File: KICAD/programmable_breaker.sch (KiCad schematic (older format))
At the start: 44 parts

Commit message: merge nicolas & stef
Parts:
- removed Q? (x2): BC847, Package_TO_SOT_SMD:SOT-23, symbol Transistor_BJT:BC847
- removed R? (x2): 10k, symbol Device:R
- removed U? (x3): LM7332, symbol Amplifier_Operational:LM7332
- added U? (x3): LM2903, Package_SO:SOIC-8-1EP_3.9x4.9mm_P1.27mm_EP2.29x3mm, symbol Comparator:LM2903
- 3214W: renamed from RV?; value R_POT -> 10K; footprint (none) -> Potentiometer_SMD:Potentiometer_Bourns_3214W_Vertical
- C? (x2): footprint (none) -> Capacitor_SMD:C_0805_2012Metric_Pad1.15x1.40mm_HandSolder
- C? (x2): value C -> 10n; footprint (none) -> Capacitor_SMD:C_0805_2012Metric_Pad1.15x1.40mm_HandSolder
- C? (x2): value 100n -> 470n; footprint (none) -> Capacitor_SMD:C_0805_2012Metric_Pad1.15x1.40mm_HandSolder
- R? (x16): footprint (none) -> Resistor_SMD:R_0805_2012Metric_Pad1.20x1.40mm_HandSolder
- R? (x2): value R -> 100k; footprint (none) -> Resistor_SMD:R_0805_2012Metric_Pad1.20x1.40mm_HandSolder
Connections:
- wire segments 89 -> 81
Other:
- note added: "comparateur courant\n(Sur-courant)"
- note removed: "Col. ouvert ?"
- note removed: "Softstart > 10ms a 100ms (le plus lent)"
- note removed: "Tres petit (Pics intempestifs) env 1ms"

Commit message: revex with jmt
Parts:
- removed SLD1, SLD2: SESAME_SHIELD, symbol Sesame:SESAME_SHIELD
- R?: value R -> 9.1k
- R?: value R -> 1k
- R? (x2): value R -> 4.7k
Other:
- note removed: "————————————————————————————————————————————————\nENTREE(S):\nTrigger quand la meusure selectionné depasse le seuil maximal\nVoltage_Sens_R | Entree Analogique | Tension mesurée du coté Droit (Provenant du block Voltage Current Sens Right)\nCurrent_Sens_R | Entree Analogique | Courant mesuré du coté Droit (Provenant du block Voltage Current Sens Right)\nVoltage_Sens_L | Entree Analogique | Tensio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"
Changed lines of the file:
@@
 $Descr A4 11693 8268
 encoding utf-8
-Sheet 5 16
+Sheet 4 16
 Title "SESAME"
 Date ""
@@
 Comment4 ""
 $EndDescr
-Text Notes 450  -300 0    50   ~ 0
-————————————————————————————————————————————————\nENTREE(S):\nTrigger quand la meusure selectionné depasse le seuil maximal\nVoltage_Sens_R | Entree Analogique | Tension mesurée du coté Droit (Provenant du block Voltage Current Sens Right)\nCurrent_Sens_R | Entree Analogique | Courant mesuré du coté Droit (Provenant du block Voltage Current Sens Right)\nVoltage_Sens_L | Entree Analogique | Tension mesurée du coté Gauche (Provenant du block Voltage Current Sens Left)\nCurrent_Sens_L | Entree Analogique | Courant mesuré du coté Gauche (Provenant du block Voltage Current Sens Left)\nDir | Entrée Numérique | Sens du courant et par extension choix de la meusure Droite / Gauche\nCurrent_Thres | Entrée ext. Analogique | Seuil externe qui definir le courant maximal\nVoltage_Thres | Entrée ext. Analogique | Seuil externe qui definir la tension maximale\nRearm | Entrée ext. Numerique | Rearmer le disjoncteur\nTrigger_Breaker | Entrée ext. Numerique | Singnal externe de declenchement du disjoncteur\n————————————————————————————————————————————————\nSORTIE(S):\nShutdown | Sortie Numerique | Signal de coupure des MOS\n
-$Comp
-L Sesame:SESAME_SHIELD SLD1
-U 2 1 618C4894
-P 5800 -1400
-F 0 "SLD1" H 5450 -1150 50  0000 L CNN
-F 1 "SESAME_SHIELD" H 5300 -1250 50  0000 L CNN
-F 2 "" H 5950 -2650 50  0001 C CNN
-F 3 "" H 5950 -2650 50  0001 C CNN
-	2    5800 -1400
-	1    0    0    -1
-$EndComp
-$Comp
-L Sesame:SESAME_SHIELD SLD2
-U 1 1 618C53DC
-P 6250 -1400
-F 0 "SLD2" H 7308 -1135 50  0000 C CNN
-F 1 "SESAME_SHIELD" H 7308 -1226 50  0000 C CNN
-F 2 "" H 6400 -2650 50  0001 C CNN
-F 3 "" H 6400 -2650 50  0001 C CNN
-	1    6250 -1400
-	1    0    0    -1
-$EndComp
-Text HLabel 5800 3200 0    50   Input ~ 0
-Rearm
 Text HLabel 2100 2400 0    50   Input ~ 0
 Voltage_Sens
@@
 Wire Wire Line
 	3000 7200 3200 7200
-Wire Wire Line
-	5800 3200 6600 3200
-Wire Wire Line
-	6600 2550 6600 3200
 Text Notes 4900 3000 2    49   ~ 0
 comparateur tension\n(Sur-tension)
@@
 Wire Wire Line
 	7400 2200 7300 2200
-Connection ~ 6600 2550
 Wire Wire Line
 	6600 2550 6850 2550
@@
 Wire Wire Line
 	7300 2550 7550 2550
-Connection ~ 7550 2550
 Wire Notes Line
 	8600 950  5900 950
@@
 P 950 2350
 F 0 "R?" H 1020 2396 50  0000 L CNN
-F 1 "R" H 1020 2305 50  0000 L CNN
+F 1 "9.1k" H 1020 2305 50  0000 L CNN
 F 2 "Resistor_SMD:R_0805_2012Metric_Pad1.20x1.40mm_HandSolder" V 880 2350 50  0001 C CNN
 F 3 "~" H 950 2350 50  0001 C CNN
@@
 P 950 2750
 F 0 "R?" H 1020 2796 50  0000 L CNN
-F 1 "R" H 1020 2705 50  0000 L CNN
+F 1 "1k" H 1020 2705 50  0000 L CNN
 F 2 "Resistor_SMD:R_0805_2012Metric_Pad1.20x1.40mm_HandSolder" V 880 2750 50  0001 C CNN
 F 3 "~" H 950 2750 50  0001 C CNN
@@
 P 950 5150
 F 0 "R?" H 1020 5196 50  0000 L CNN
-F 1 "R" H 1020 5105 50  0000 L CNN
+F 1 "4.7k" H 1020 5105 50  0000 L CNN
 F 2 "Resistor_SMD:R_0805_2012Metric_Pad1.20x1.40mm_HandSolder" V 880 5150 50  0001 C CNN
 F 3 "~" H 950 5150 50  0001 C CNN
@@
 P 950 5550
 F 0 "R?" H 1020 5596 50  0000 L CNN
-F 1 "R" H 1020 5505 50  0000 L CNN
+F 1 "4.7k" H 1020 5505 50  0000 L CNN
 F 2 "Resistor_SMD:R_0805_2012Metric_Pad1.20x1.40mm_HandSolder" V 880 5550 50  0001 C CNN
 F 3 "~" H 950 5550 50  0001 C CNN
@@
 $EndComp
 Wire Wire Line
-	7550 2550 7550 4550
-Wire Wire Line
 	4700 4550 5450 4550
 Wire Wire Line
@@
 Connection ~ 5450 4550
 Wire Wire Line
-	5450 4550 7550 4550
+	5450 4550 6850 4550
 $Comp
 L Comparator:LM2903 U?
@@
 	1    0    0    -1
 $EndComp
+Text HLabel 6650 4750 0    50   Input ~ 0
+Rearm
+Wire Wire Line
+	6850 2550 6850 4550
+Connection ~ 6850 2550
+Connection ~ 7300 2550
+Wire Wire Line
+	6650 4750 7300 4750
+Wire Wire Line
+	7300 2550 7300 4750
 $EndSCHEMATC

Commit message: minor cleanup
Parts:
- gave numbers to parts that had none: 1
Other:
- moved on the sheet: C?, R?
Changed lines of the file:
@@
 $Descr A4 11693 8268
 encoding utf-8
-Sheet 4 16
+Sheet 3 16
 Title "SESAME"
 Date ""
@@
 Text HLabel 2100 4450 0    50   Input ~ 0
 Current_Thres
-Text HLabel 2100 5200 0    50   Input ~ 0
+Text HLabel 2150 4850 0    50   Input ~ 0
 Current_Sens
 Wire Notes Line
@@
 L Device:R R?
 U 1 1 615178DC
-P 3000 5200
-F 0 "R?" V 3200 5200 50  0000 C CNN
-F 1 "100k" V 3100 5200 50  0000 C CNN
-F 2 "Resistor_SMD:R_0805_2012Metric_Pad1.20x1.40mm_HandSolder" V 2930 5200 50  0001 C CNN
-F 3 "~" H 3000 5200 50  0001 C CNN
-	1    3000 5200
+P 3000 4850
+F 0 "R?" V 3200 4850 50  0000 C CNN
+F 1 "100k" V 3100 4850 50  0000 C CNN
+F 2 "Resistor_SMD:R_0805_2012Metric_Pad1.20x1.40mm_HandSolder" V 2930 4850 50  0001 C CNN
+F 3 "~" H 3000 4850 50  0001 C CNN
+	1    3000 4850
 	0    1    1    0
 $EndComp
@@
 L Device:C C?
 U 1 1 615178FE
-P 3450 5450
-F 0 "C?" H 3565 5496 50  0000 L CNN
-F 1 "10n" H 3565 5405 50  0000 L CNN
-F 2 "Capacitor_SMD:C_0805_2012Metric_Pad1.15x1.40mm_HandSolder" H 3488 5300 50  0001 C CNN
-F 3 "~" H 3450 5450 50  0001 C CNN
-	1    3450 5450
-	1    0    0    -1
-$EndComp
-Wire Wire Line
-	3450 4650 3450 5200
+P 3450 5100
+F 0 "C?" H 3565 5146 50  0000 L CNN
+F 1 "10n" H 3565 5055 50  0000 L CNN
+F 2 "Capacitor_SMD:C_0805_2012Metric_Pad1.15x1.40mm_HandSolder" H 3488 4950 50  0001 C CNN
+F 3 "~" H 3450 5100 50  0001 C CNN
+	1    3450 5100
+	1    0    0    -1
+$EndComp
+Wire Wire Line
+	3450 4650 3450 4850
 $Comp
 L power:GND #PWR0151
 U 1 1 61517905
-P 3450 5600
-F 0 "#PWR0151" H 3450 5350 50  0001 C CNN
-F 1 "GND" H 3455 5427 50  0000 C CNN
-F 2 "" H 3450 5600 50  0001 C CNN
-F 3 "" H 3450 5600 50  0001 C CNN
-	1    3450 5600
+P 3450 5250
+F 0 "#PWR0151" H 3450 5000 50  0001 C CNN
+F 1 "GND" H 3455 5077 50  0000 C CNN
+F 2 "" H 3450 5250 50  0001 C CNN
+F 3 "" H 3450 5250 50  0001 C CNN
+	1    3450 5250
 	1    0    0    -1
 $EndComp
@@
 $EndComp
 Wire Wire Line
-	3450 5200 3150 5200
-Connection ~ 3450 5200
-Wire Wire Line
-	3450 5200 3450 5300
+	3450 4850 3150 4850
+Connection ~ 3450 4850
+Wire Wire Line
+	3450 4850 3450 4950
 Wire Wire Line
 	2100 4450 2300 4450
 Wire Wire Line
-	2100 5200 2850 5200
+	2150 4850 2850 4850
 Wire Notes Line
 	2200 3300 4950 3300
@@
 	1400 4700 1400 6200
 $Comp
-L Comparator:LM2903 U?
+L Comparator:LM2903 U7
 U 1 1 611D87A4
 P 4400 1750
-F 0 "U?" H 4400 2117 50  0000 C CNN
+F 0 "U7" H 4400 2117 50  0000 C CNN
 F 1 "LM2903" H 4400 2026 50  0000 C CNN
 F 2 "Package_SO:SOIC-8-1EP_3.9x4.9mm_P1.27mm_EP2.29x3mm" H 4400 1750 50  0001 C CNN
@@
 	4700 1750 5450 1750
 $Comp
-L Comparator:LM2903 U?
+L Comparator:LM2903 U7
 U 2 1 611EA33A
 P 4400 4550
-F 0 "U?" H 4400 4917 50  0000 C CNN
+F 0 "U7" H 4400 4917 50  0000 C CNN
 F 1 "LM2903" H 4400 4826 50  0000 C CNN
 F 2 "Package_SO:SOIC-8-1EP_3.9x4.9mm_P1.27mm_EP2.29x3mm" H 4400 4550 50  0001 C CNN
@@
 	5450 4550 6850 4550
 $Comp
-L Comparator:LM2903 U?
+L Comparator:LM2903 U7
 U 3 1 6120EB61
 P 2900 6850
-F 0 "U?" H 2550 6950 50  0000 L CNN
+F 0 "U7" H 2550 6950 50  0000 L CNN
 F 1 "LM2903" H 2450 6800 50  0000 L CNN
 F 2 "Package_SO:SOIC-8-1EP_3.9x4.9mm_P1.27mm_EP2.29x3mm" H 2900 6850 50  0001 C CNN

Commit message: Stef merge
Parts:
- added TP?: TP_NOT, symbol Connector:TestPoint
- added TP?: TP_NOP, symbol Connector:TestPoint
- added TP? (x2): TP_POP, symbol Connector:TestPoint
- C? (x6): footprint Capacitor_SMD:C_0805_2012Metric_Pad1.15x1.40mm_HandSolder -> Capacitor_SMD:C_0805_2012Metric
- R? (x14): footprint Resistor_SMD:R_0805_2012Metric_Pad1.20x1.40mm_HandSolder -> Resistor_SMD:R_0805_2012Metric
- R?: value 9.1k -> R; footprint Resistor_SMD:R_0805_2012Metric_Pad1.20x1.40mm_HandSolder -> Resistor_SMD:R_0805_2012Metric
- R?: value 1k -> R; footprint Resistor_SMD:R_0805_2012Metric_Pad1.20x1.40mm_HandSolder -> Resistor_SMD:R_0805_2012Metric
- R? (x2): value 4.7k -> R; footprint Resistor_SMD:R_0805_2012Metric_Pad1.20x1.40mm_HandSolder -> Resistor_SMD:R_0805_2012Metric
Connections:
- net Over_UI_Protection: now also TP?.1
- net at Q?.1 (B), R?.1, U7.1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: now also TP?.1
- net at C?.2, JP?.2, JP?.2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: now also TP?.1 (x2)
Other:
- note added: "Signal amp. & Invert"
- note removed: "Inversion + amplification du signal"
- moved on the sheet: C?, Q?, R?, U7C

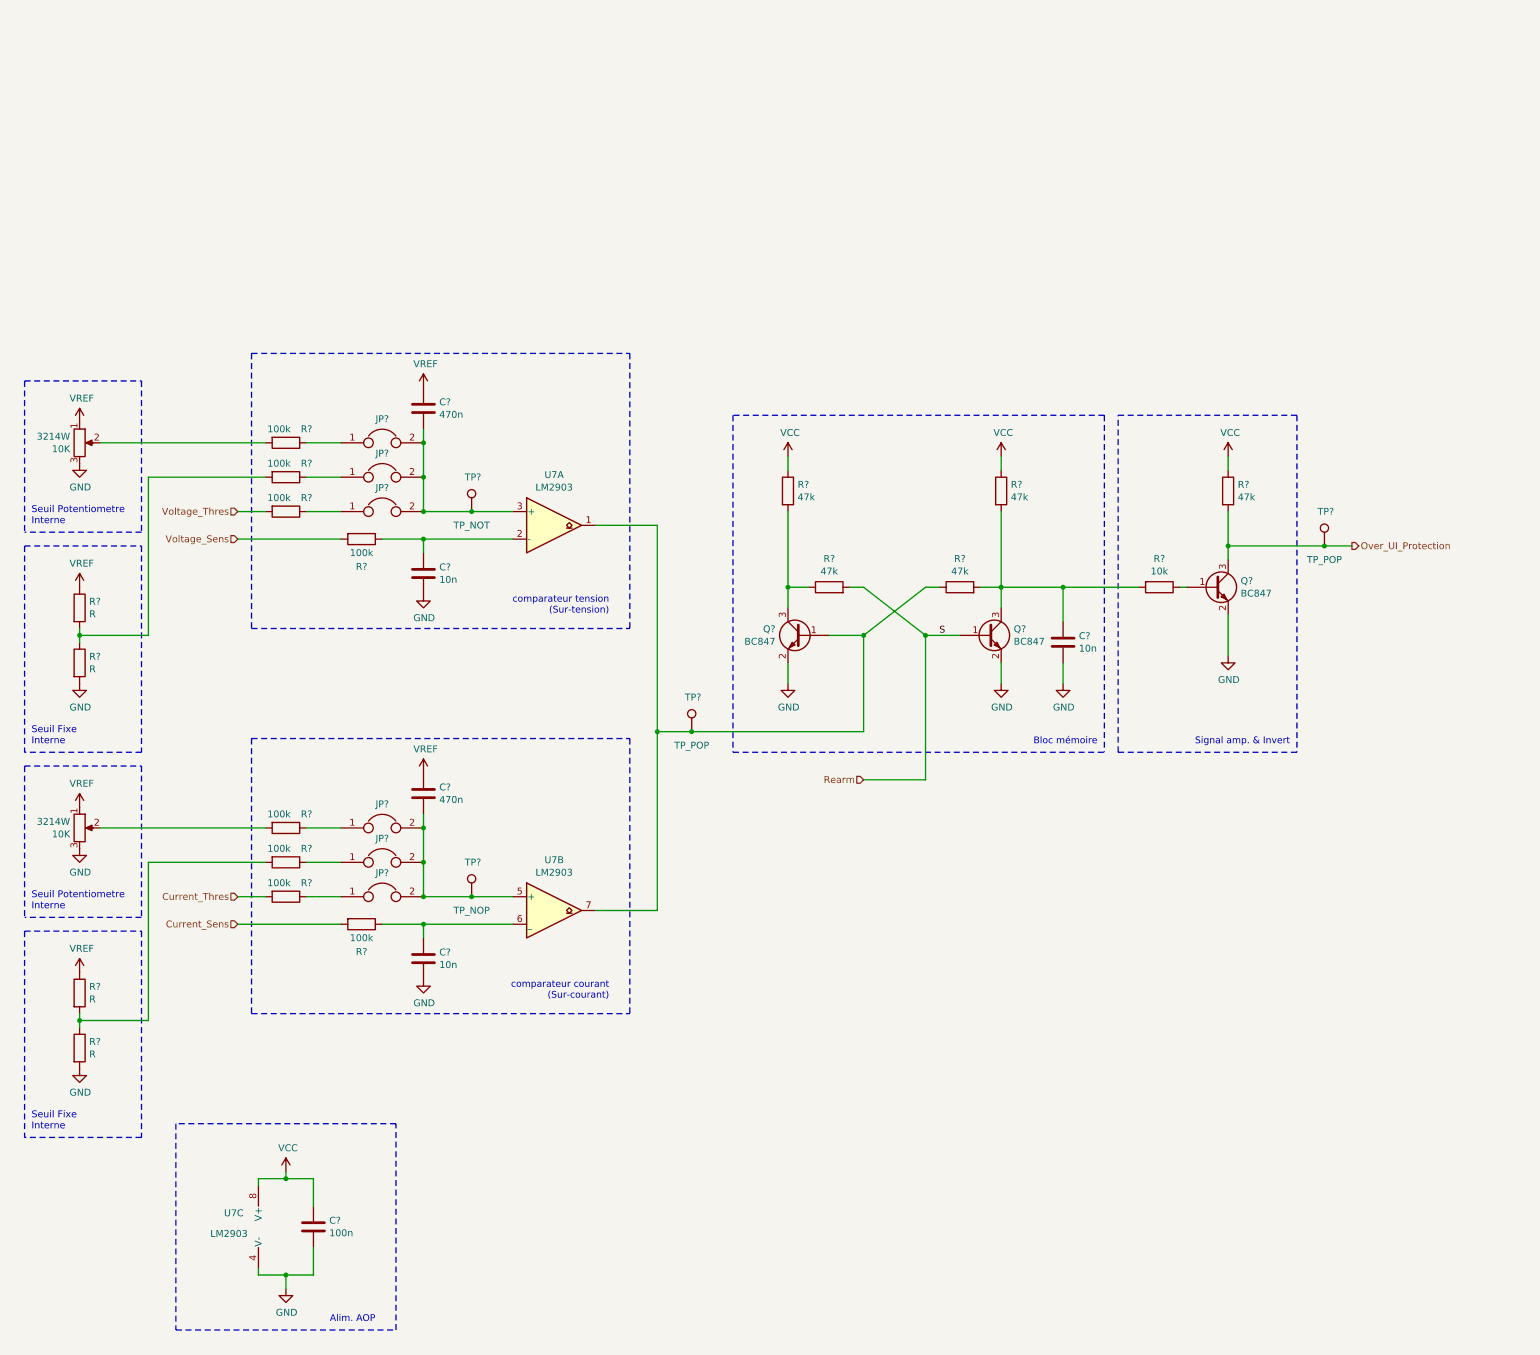
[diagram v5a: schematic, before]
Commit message: drivers draft + clean and minors changes
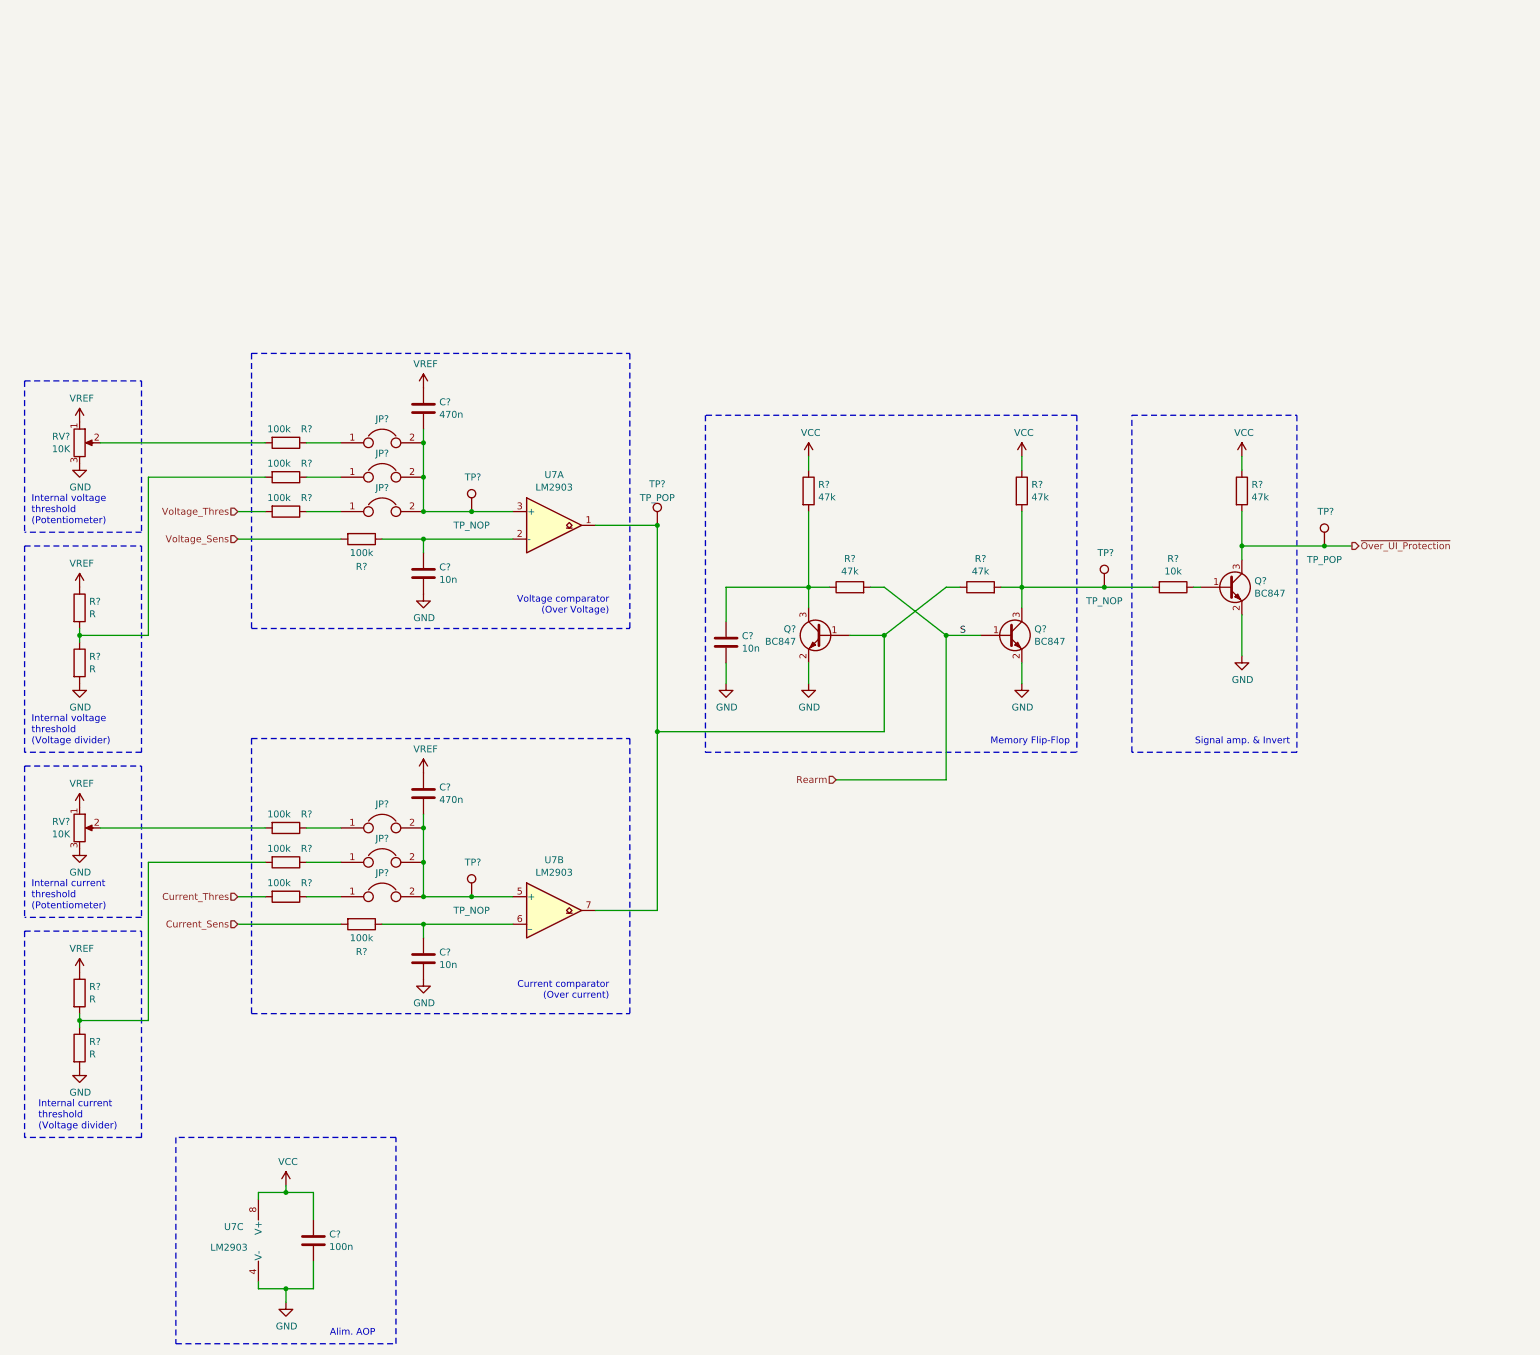
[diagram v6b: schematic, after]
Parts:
- removed TP?: TP_POP, symbol Connector:TestPoint
- added TP?: TP_NOP, symbol Connector:TestPoint
- added TP?: TP_POP, symbol Connector:TestPoint
- C? (x6): footprint Capacitor_SMD:C_0805_2012Metric -> Capacitor_SMD:C_0805_2012Metric_Pad1.15x1.40mm_HandSolder
- R? (x18): footprint Resistor_SMD:R_0805_2012Metric -> Resistor_SMD:R_0805_2012Metric_Pad1.15x1.40mm_HandSolder
- RV? (x2): renamed from 3214W; Manifacturer_Ref (none) -> 3214W
- TP?: value TP_NOT -> TP_NOP
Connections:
- net at Q?.3 (C), R?.1, R?.2: now also C?.1
- net at Q?.1 (B), R?.1, U7.1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: now also TP?.1
- net at Q?.3 (C), R?.2, R?.2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: now also TP?.1; no longer C?.1
- net Over_UI_Protection renamed ~Over_UI_Protection
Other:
- note added: "Current comparator\n(Over current)"
- note added: "Internal current\nthreshold\n(Potentiometer)"
- note added: "Internal current\nthreshold\n(Voltage divider)"
- note added: "Internal voltage\nthreshold\n(Potentiometer)"
- note added: "Internal voltage\nthreshold\n(Voltage divider)"
- note added: "Memory Flip-Flop"
- note added: "Voltage comparator\n(Over Voltage)"
- note removed: "Bloc mémoire"
- note removed: "Seuil Fixe\nInterne"
- note removed: "Seuil Potentiometre\nInterne"
- note removed: "comparateur courant\n(Sur-courant)"
- note removed: "comparateur tension\n(Sur-tension)"
- moved on the sheet: C?, Q?, R?, U7C

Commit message: driver + clean clean clean
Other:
- moved on the sheet: C?
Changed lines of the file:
@@
 $Descr A4 11693 8268
 encoding utf-8
-Sheet 3 16
+Sheet 3 17
 Title "SESAME"
 Date ""
@@
 L Device:C C?
 U 1 1 610FF241
-P 5650 2600
-F 0 "C?" H 5765 2646 50  0000 L CNN
-F 1 "10n" H 5765 2555 50  0000 L CNN
-F 2 "Capacitor_SMD:C_0805_2012Metric_Pad1.15x1.40mm_HandSolder" H 5688 2450 50  0001 C CNN
-F 3 "~" H 5650 2600 50  0001 C CNN
-	1    5650 2600
+P 5800 2600
+F 0 "C?" H 5550 2650 50  0000 L CNN
+F 1 "10n" H 5550 2550 50  0000 L CNN
+F 2 "Capacitor_SMD:C_0805_2012Metric_Pad1.15x1.40mm_HandSolder" H 5838 2450 50  0001 C CNN
+F 3 "~" H 5800 2600 50  0001 C CNN
+	1    5800 2600
 	1    0    0    -1
 $EndComp
@@
 L power:GND #PWR012
 U 1 1 6110DB40
-P 5650 2900
-F 0 "#PWR012" H 5650 2650 50  0001 C CNN
-F 1 "GND" H 5655 2727 50  0000 C CNN
-F 2 "" H 5650 2900 50  0001 C CNN
-F 3 "" H 5650 2900 50  0001 C CNN
-	1    5650 2900
+P 5800 2900
+F 0 "#PWR012" H 5800 2650 50  0001 C CNN
+F 1 "GND" H 5805 2727 50  0000 C CNN
+F 2 "" H 5800 2900 50  0001 C CNN
+F 3 "" H 5800 2900 50  0001 C CNN
+	1    5800 2900
 	1    0    0    -1
 $EndComp
@@
 	9050 2200 9100 2200
 Wire Wire Line
-	5650 2900 5650 2750
+	5800 2900 5800 2750
 Wire Notes Line
 	5500 3400 8200 3400
@@
 	950  2550 950  2500
 Wire Wire Line
-	5650 2450 5650 2200
+	5800 2450 5800 2200
 Wire Notes Line
 	8600 3400 8600 950
@@
 	7800 2200 8400 2200
 Wire Wire Line
-	5650 2200 6250 2200
+	5800 2200 6250 2200
 Wire Wire Line
 	5150 3250 6800 3250

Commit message: review w/ jmt
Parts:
- added C?: 100n, symbol Device:C
- added R?: 1k, symbol Device:R
- C10, C11, C6, C7, C8, C9: renamed from C?; footprint Capacitor_SMD:C_0805_2012Metric_Pad1.15x1.40mm_HandSolder -> (none)
- R10, R11, R12, R13, R14, R15, R16, R17, R18, R19, R20, R21, R22, R23, R24, R25, R26, R27: renamed from R?; footprint Resistor_SMD:R_0805_2012Metric_Pad1.15x1.40mm_HandSolder -> (none)
- U2: renamed from U7; footprint Package_SO:SOIC-8-1EP_3.9x4.9mm_P1.27mm_EP2.29x3mm -> (none)
- gave numbers to parts that had none: 16
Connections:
- net VCC: now also C?.1
- net ~Over_UI_Protection: now also C?.2, R?.1; no longer Q3.3 (C), R27.2, TP9.1
- new net: Q3.3 (C), R27.2, R?.2, TP9.1
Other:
- note added: "au plus vite (juste apres le triangle)\nenv 0.1ms"
- moved on the sheet: C10, C11, C7, C8, C9, JP4, JP5, JP6, JP7, JP8, JP9, Q1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
